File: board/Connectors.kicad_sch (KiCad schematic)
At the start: 17 parts, among them J10 SLOT 1, J11 SLOT 2, J12 SLOT 3, J13 SLOT 4, J14 SLOT 5, J15 AudioJack3, J16 SPI Device 0, J18 SPI Device 1, J19 SPI Device 2, J20 SPI Device 3, J21 SPI Device 4, J22 SPI Device 5, J23 SPI Device 6, J24 SPI Device 7, J25 VIA Port A, J26 SP720APP, J9 SLOT 0

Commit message: Board V1.1G
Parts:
- J15: footprint Connector_Audio:Jack_3.5mm_CUI_SJ1-3523N_Horizontal -> Connector_Audio:Jack_3.5mm_CUI_SJ1-3525N_Horizontal
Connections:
- net A0 renamed A_SLOTS0
- net A1 renamed A_SLOTS1
- net A10 renamed A_SLOTS10
- net A11 renamed A_SLOTS11
- net A12 renamed A_SLOTS12
- net A13 renamed A_SLOTS13
- net A14 renamed A_SLOTS14
- net A15 renamed A_SLOTS15
- net A2 renamed A_SLOTS2
- net A3 renamed A_SLOTS3
- net A4 renamed A_SLOTS4
- net A5 renamed A_SLOTS5
- net A6 renamed A_SLOTS6
- net A7 renamed A_SLOTS7
- net A8 renamed A_SLOTS8
- net A9 renamed A_SLOTS9
- net D0 renamed D_SLOTS0
- net D1 renamed D_SLOTS1
- net D2 renamed D_SLOTS2
- net D3 renamed D_SLOTS3
- net D4 renamed D_SLOTS4
- net D5 renamed D_SLOTS5
- net D6 renamed D_SLOTS6
- net D7 renamed D_SLOTS7
- net RWB renamed P_RWB
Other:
- moved on the sheet: J10, J11, J12, J13, J14, J15, J16, J18, J19, J20, J21, J22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

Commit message: V1.2B: Final for production.
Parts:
- J15: value AudioJack3 -> Audio Jack
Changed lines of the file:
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@@
 		(title "Card-edge and SPI Device Connectors")
 		(date "2025-03-04")
-		(rev "1.1A")
+		(rev "1.3B")
 		(company "Data Tuning")
 		(comment 1 "Hydra 16")
@@
 			)
 		)
-		(property "Value" "AudioJack3"
+		(property "Value" "Audio Jack"
 			(at 200.66 165.7349 0)
 			(effects

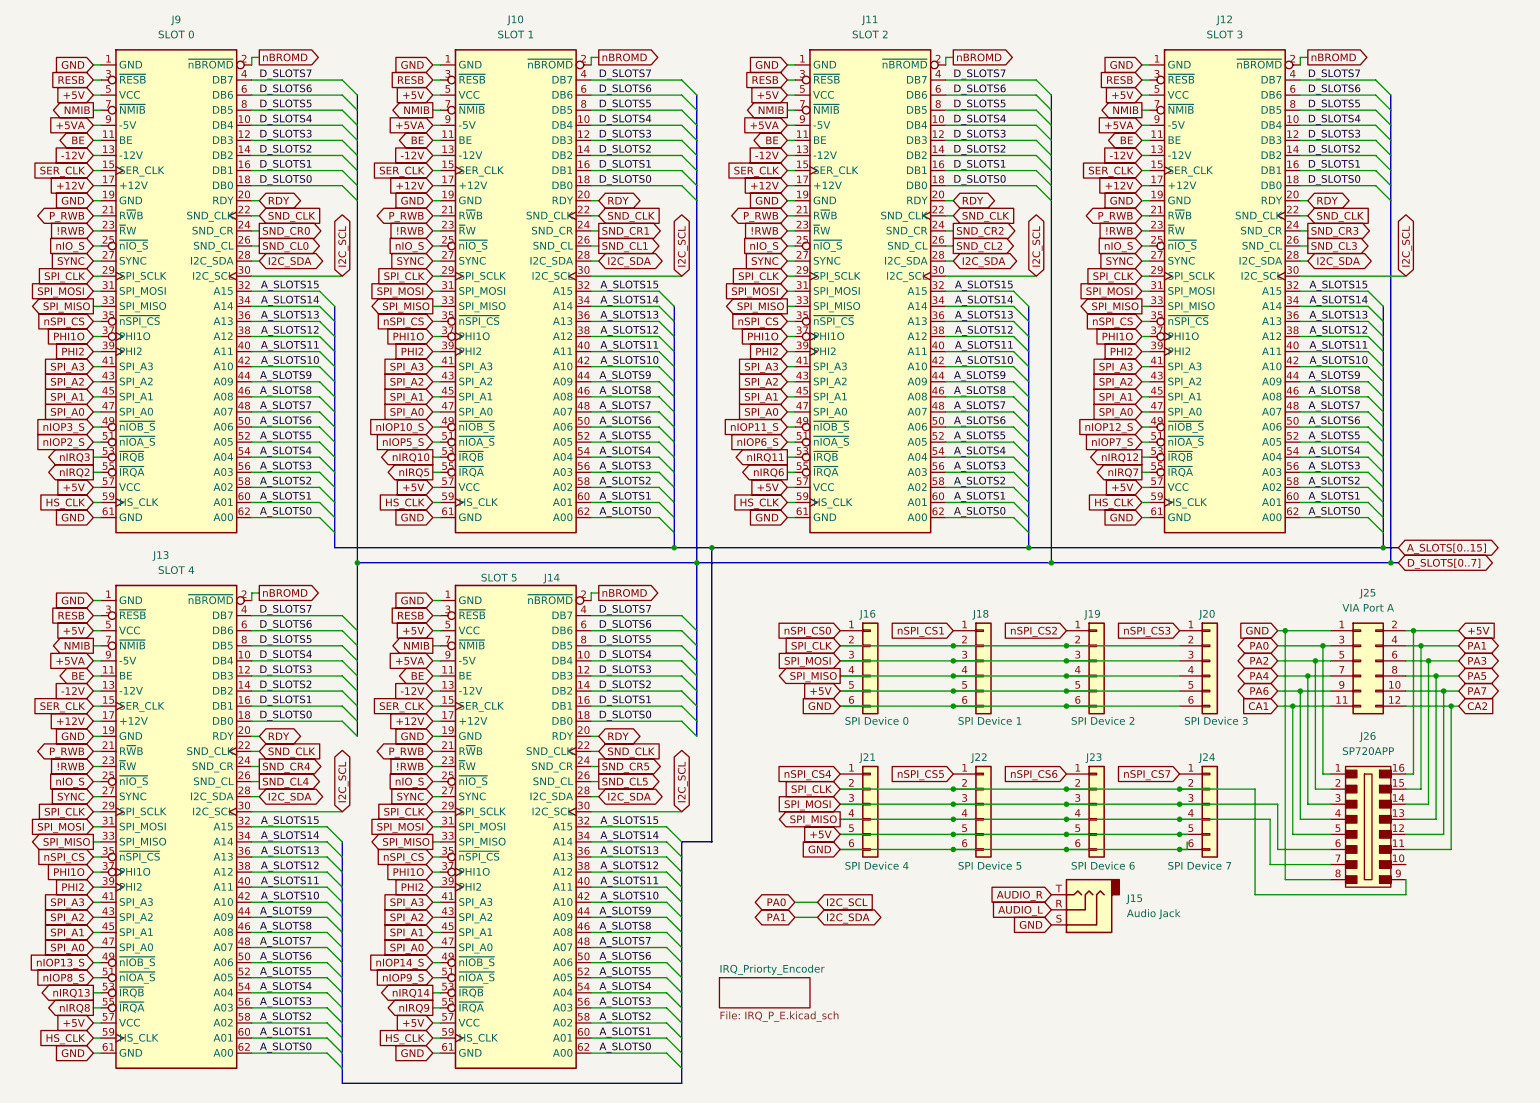
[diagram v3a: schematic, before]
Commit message: V1.3C without board traces
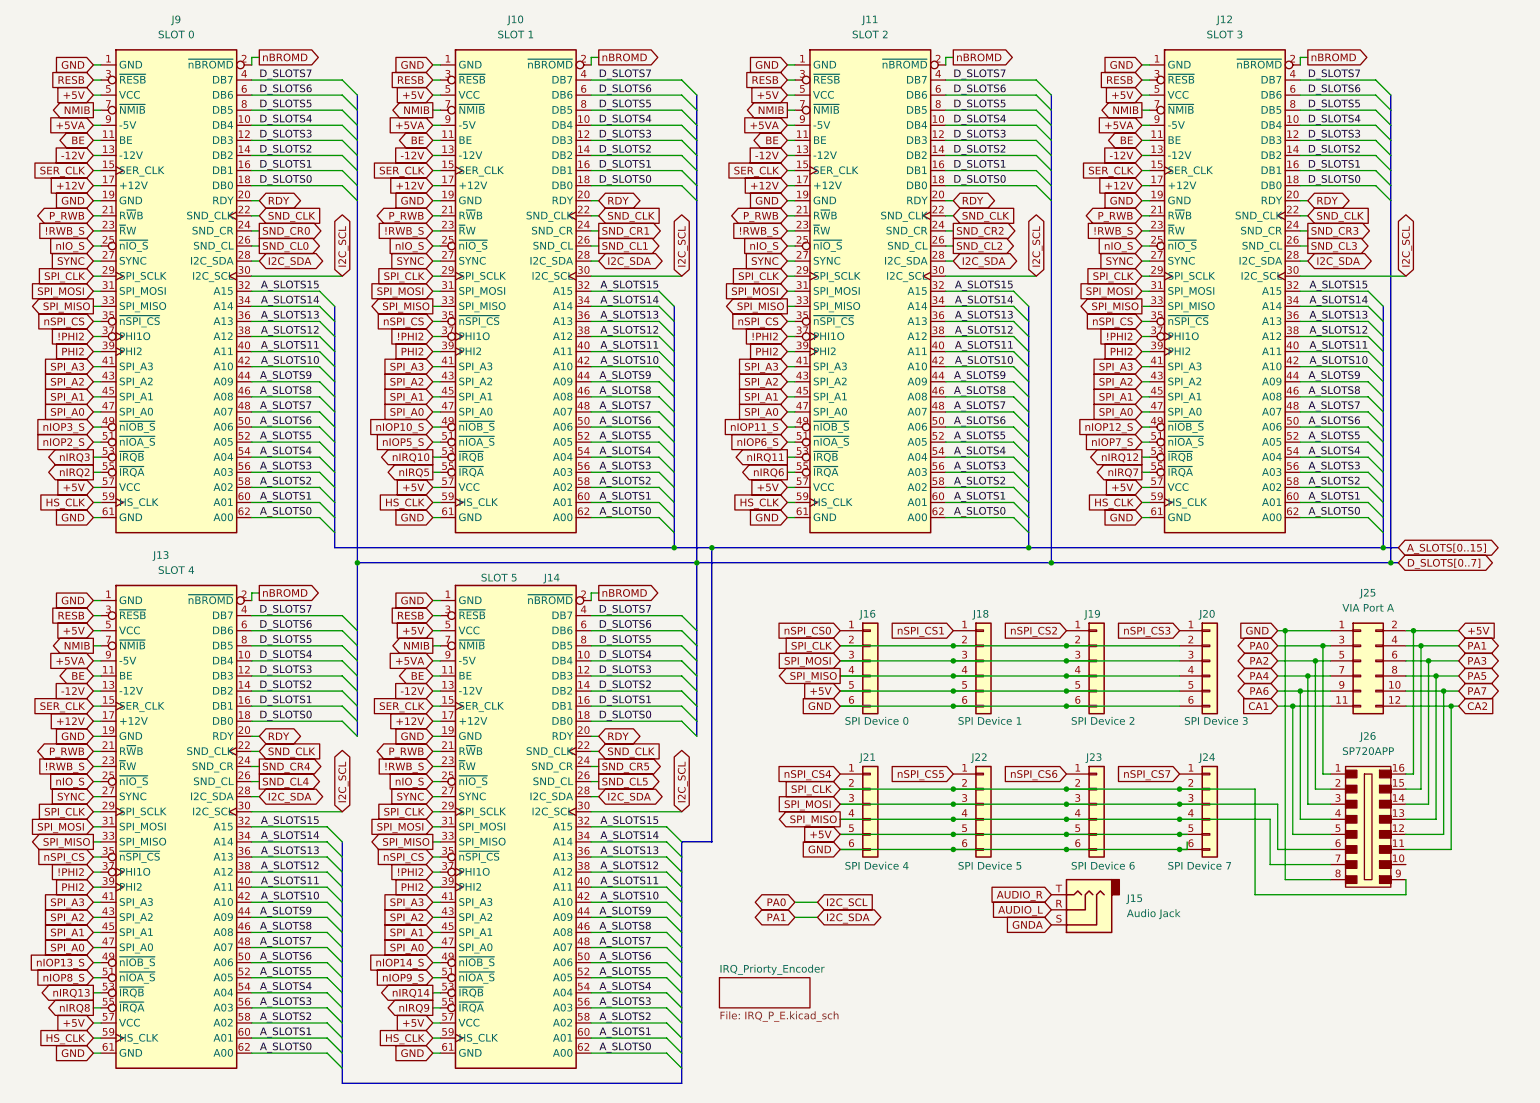
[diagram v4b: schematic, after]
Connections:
- net GND: no longer J15.S
- net !RWB renamed !RWB_S
- net PHI1O renamed !PHI2
- new net GNDA: J15.S
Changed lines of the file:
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@@
 	(title_block
 		(title "Card-edge and SPI Device Connectors")
-		(date "2025-04-15")
-		(rev "1.3")
+		(date "2025-04-23")
+		(rev "1.3C")
 		(company "Data Tuning")
 		(comment 1 "Hydra 16")
@@
 		)
 	)
-	(global_label "PHI1O"
+	(global_label "!PHI2"
 		(shape input)
 		(at 143.51 68.58 180)
@@
 		)
 		(property "Intersheetrefs" "${INTERSHEET_REFS}"
-			(at 134.7795 68.58 0)
+			(at 135.5052 68.58 0)
 			(effects
 				(font
@@
 		)
 	)
-	(global_label "!RWB"
+	(global_label "!RWB_S"
 		(shape input)
 		(at 83.82 140.97 180)
@@
 		)
 		(property "Intersheetrefs" "${INTERSHEET_REFS}"
-			(at 76.2386 140.97 0)
+			(at 74.0615 140.97 0)
 			(effects
 				(font
@@
 		)
 	)
-	(global_label "!RWB"
+	(global_label "!RWB_S"
 		(shape input)
 		(at 26.67 140.97 180)
@@
 		)
 		(property "Intersheetrefs" "${INTERSHEET_REFS}"
-			(at 19.0886 140.97 0)
+			(at 16.9115 140.97 0)
 			(effects
 				(font
@@
 		)
 	)
-	(global_label "PHI1O"
+	(global_label "!PHI2"
 		(shape input)
 		(at 83.82 68.58 180)
@@
 		)
 		(property "Intersheetrefs" "${INTERSHEET_REFS}"
-			(at 75.0895 68.58 0)
+			(at 75.8152 68.58 0)
 			(effects
 				(font
@@
 		)
 	)
-	(global_label "GND"
+	(global_label "GNDA"
 		(shape input)
 		(at 187.96 167.64 180)
@@
 		)
 		(property "Intersheetrefs" "${INTERSHEET_REFS}"
-			(at 181.1043 167.64 0)
+			(at 180.0157 167.64 0)
 			(effects
 				(font
@@
 		)
 	)
-	(global_label "!RWB"
+	(global_label "!RWB_S"
 		(shape input)
 		(at 203.2 50.8 180)
@@
 		)
 		(property "Intersheetrefs" "${INTERSHEET_REFS}"
-			(at 195.6186 50.8 0)
+			(at 193.4415 50.8 0)
 			(effects
 				(font
@@
 		)
 	)
-	(global_label "PHI1O"
+	(global_label "!PHI2"
 		(shape input)
 		(at 26.67 68.58 180)
@@
 		)
 		(property "Intersheetrefs" "${INTERSHEET_REFS}"
-			(at 17.9395 68.58 0)
+			(at 18.6652 68.58 0)
 			(effects
 				(font
@@
 		)
 	)
-	(global_label "!RWB"
+	(global_label "!RWB_S"
 		(shape input)
 		(at 26.67 50.8 180)
@@
 		)
 		(property "Intersheetrefs" "${INTERSHEET_REFS}"
-			(at 19.0886 50.8 0)
+			(at 16.9115 50.8 0)
 			(effects
 				(font
@@
 		)
 	)
-	(global_label "PHI1O"
+	(global_label "!PHI2"
 		(shape input)
 		(at 203.2 68.58 180)
@@
 		)
 		(property "Intersheetrefs" "${INTERSHEET_REFS}"
-			(at 194.4695 68.58 0)
+			(at 195.1952 68.58 0)
 			(effects
 				(font
@@
 		)
 	)
-	(global_label "PHI1O"
+	(global_label "!PHI2"
 		(shape input)
 		(at 26.67 158.75 180)
@@
 		)
 		(property "Intersheetrefs" "${INTERSHEET_REFS}"
-			(at 17.9395 158.75 0)
+			(at 18.6652 158.75 0)
 			(effects
 				(font
@@
 		)
 	)
-	(global_label "!RWB"
+	(global_label "!RWB_S"
 		(shape input)
 		(at 83.82 50.8 180)
@@
 		)
 		(property "Intersheetrefs" "${INTERSHEET_REFS}"
-			(at 76.2386 50.8 0)
+			(at 74.0615 50.8 0)
 			(effects
 				(font
@@
 		)
 	)
-	(global_label "PHI1O"
+	(global_label "!PHI2"
 		(shape input)
 		(at 83.82 158.75 180)
@@
 		)
 		(property "Intersheetrefs" "${INTERSHEET_REFS}"
-			(at 75.0895 158.75 0)
+			(at 75.8152 158.75 0)
 			(effects
 				(font
@@
 		)
 	)
-	(global_label "!RWB"
+	(global_label "!RWB_S"
 		(shape input)
 		(at 143.51 50.8 180)
@@
 		)
 		(property "Intersheetrefs" "${INTERSHEET_REFS}"
-			(at 135.9286 50.8 0)
+			(at 133.7515 50.8 0)
 			(effects
 				(font

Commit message: V1.4E
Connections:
- net A_SLOTS0 renamed A0
- net A_SLOTS1 renamed A1
- net A_SLOTS10 renamed A10
- net A_SLOTS11 renamed A11
- net A_SLOTS12 renamed A12
- net A_SLOTS13 renamed A13
- net A_SLOTS14 renamed A14
- net A_SLOTS15 renamed A15
- net A_SLOTS2 renamed A2
- net A_SLOTS3 renamed A3
- net A_SLOTS4 renamed A4
- net A_SLOTS5 renamed A5
- net A_SLOTS6 renamed A6
- net A_SLOTS7 renamed A7
- net A_SLOTS8 renamed A8
- net A_SLOTS9 renamed A9
- net D_SLOTS0 renamed D0
- net D_SLOTS1 renamed D1
- net D_SLOTS2 renamed D2
- net D_SLOTS3 renamed D3
- net D_SLOTS4 renamed D4
- net D_SLOTS5 renamed D5
- net D_SLOTS6 renamed D6
- net D_SLOTS7 renamed D7

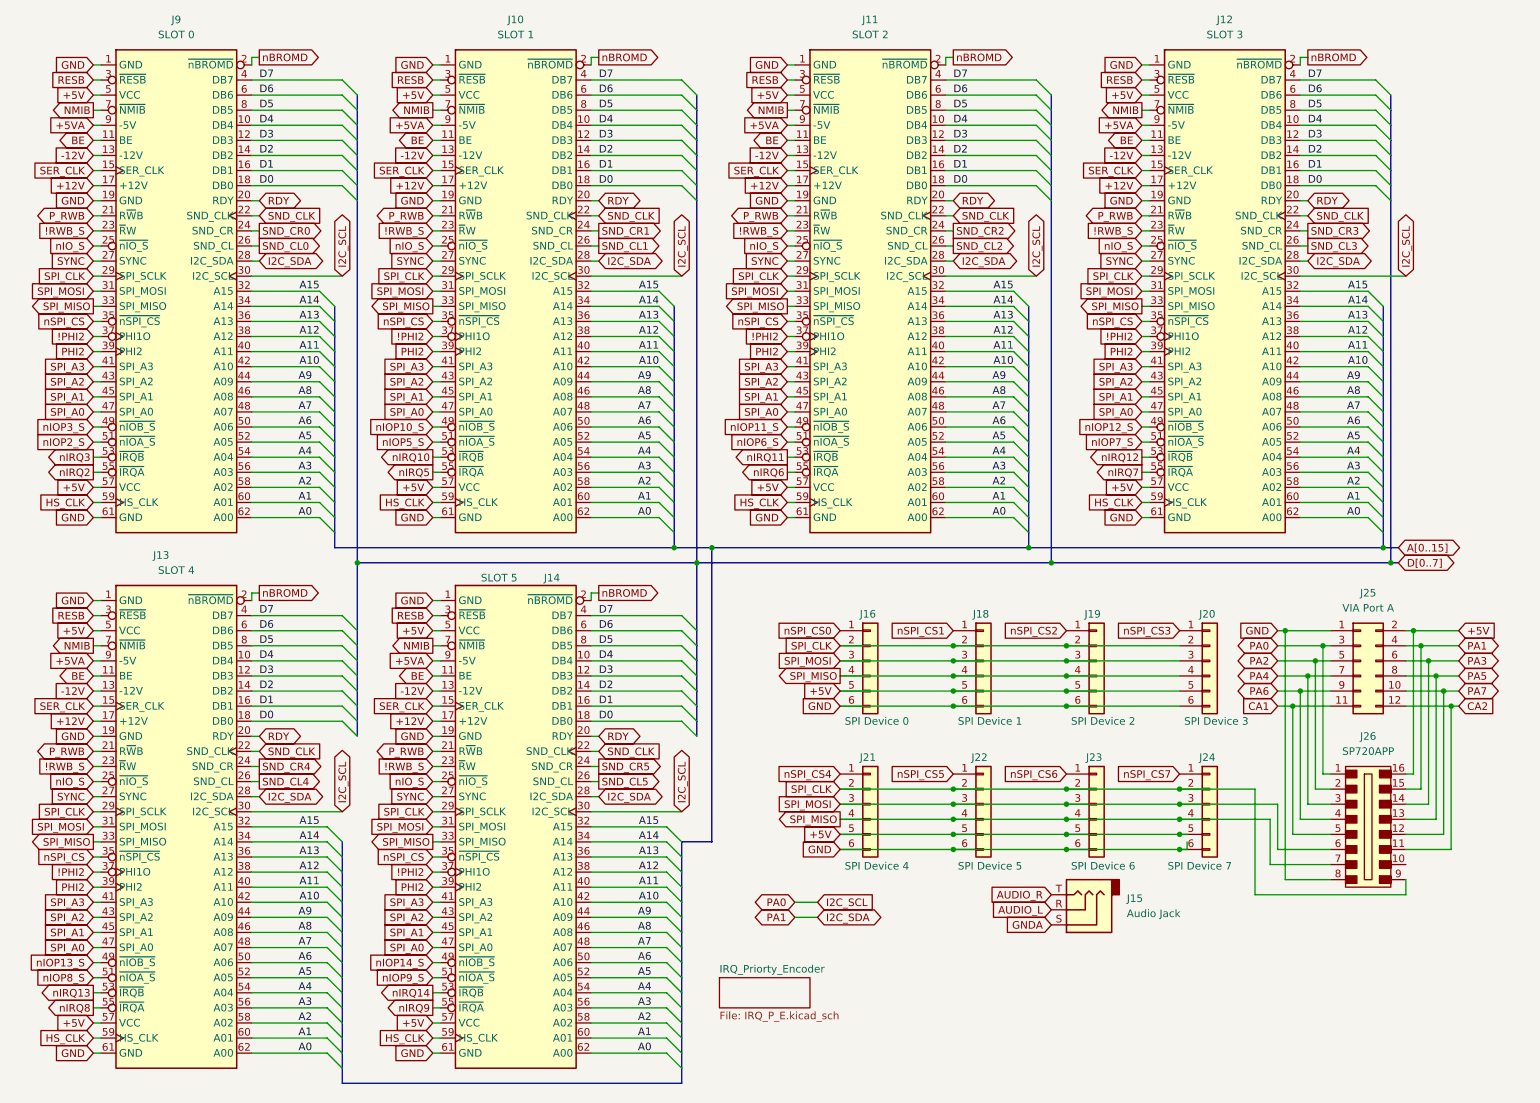
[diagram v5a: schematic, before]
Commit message: Version 1.7A: More rearrangement, partial wiring of PDB, addition of W register
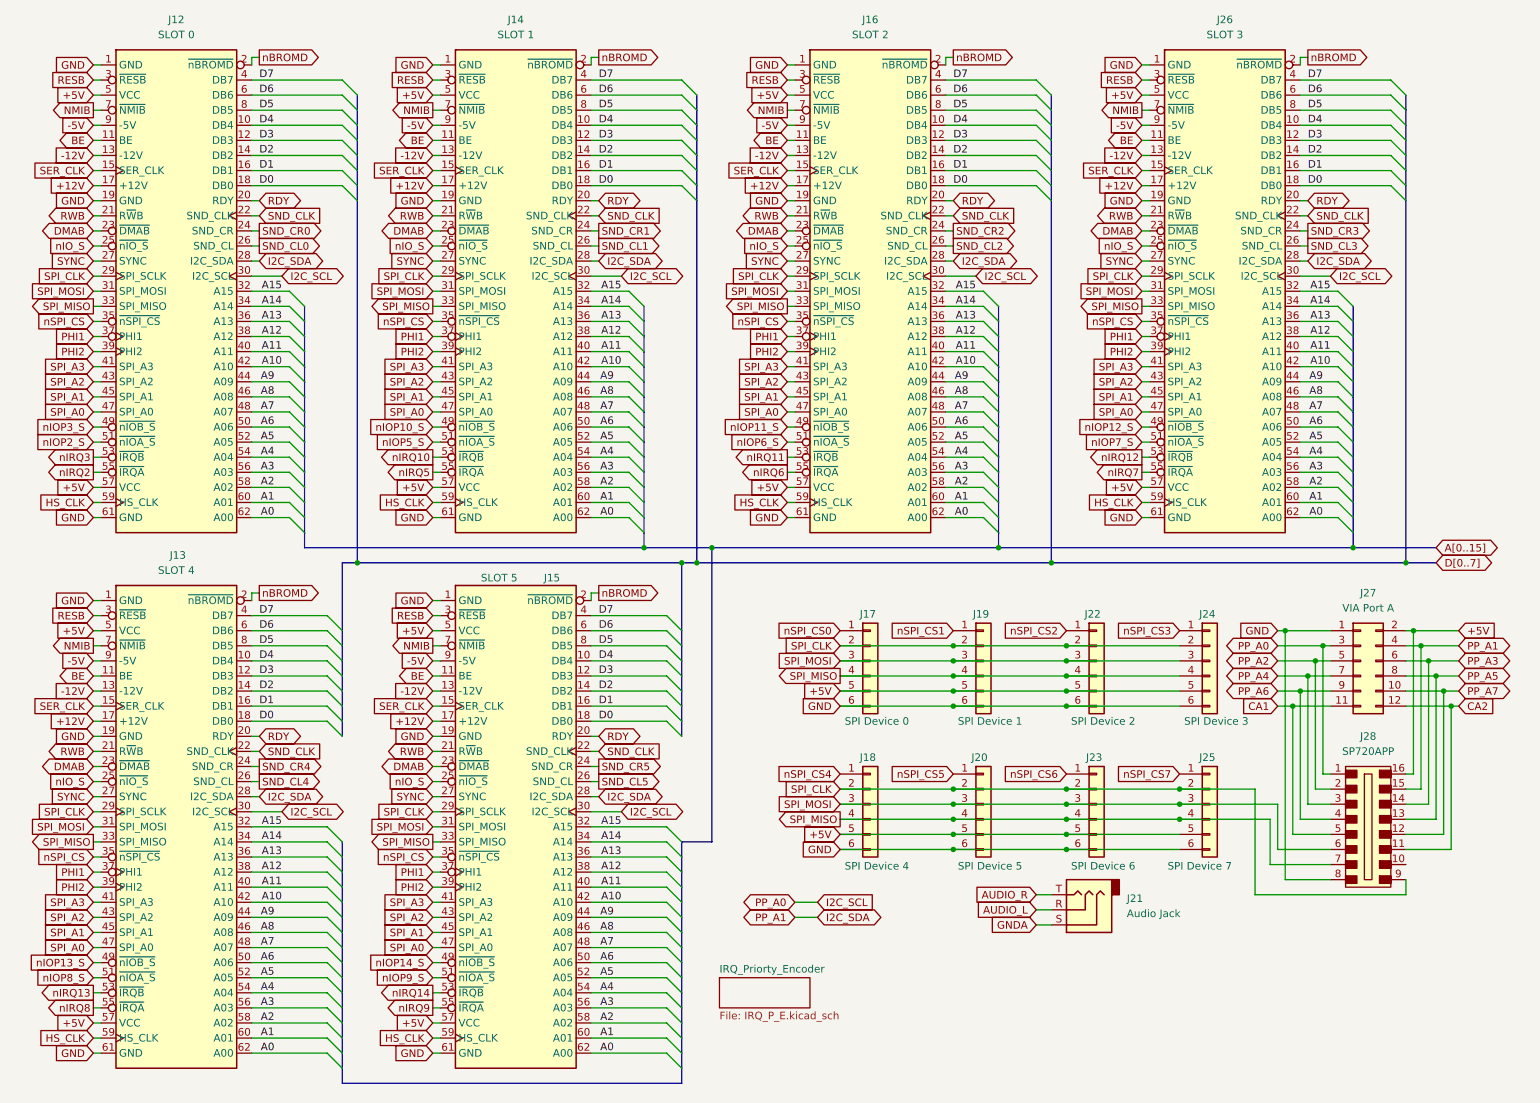
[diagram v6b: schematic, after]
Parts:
- renumbered J9 to J12, J10 to J14, J14 to J15, J11 to J16, J16 to J17, J21 to J18, J18 to J19, J22 to J20, J15 to J21, J19 to J22, J20 to J24, J24 to J25, J12 to J26, J25 to J27, J26 to J28
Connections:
- net !PHI2 renamed PHI1
- net !RWB_S renamed DMAB
- net +5VA renamed -5V
- net PA2 renamed PP_A2
- net PA3 renamed PP_A3
- net PA4 renamed PP_A4
- net PA5 renamed PP_A5
- net PA6 renamed PP_A6
- net PA7 renamed PP_A7
- net P_RWB renamed RWB

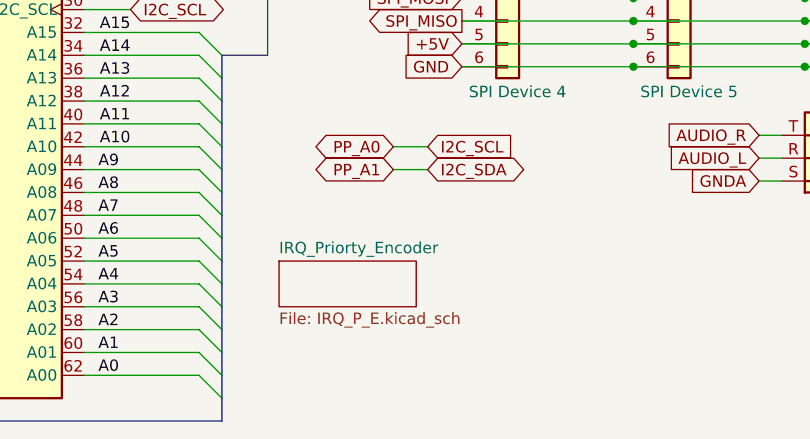
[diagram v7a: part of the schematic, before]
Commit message: 1.7C: Logic corrections and placement tweaks
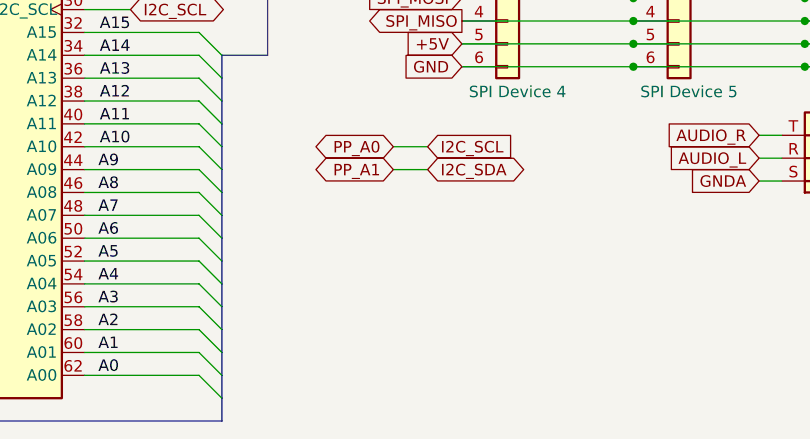
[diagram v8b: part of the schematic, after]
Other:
- removed sheet IRQ_Priorty_Encoder
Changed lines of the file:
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@@
 	(title_block
 		(title "Card-edge and SPI Device Connectors")
-		(date "2025-09-18")
-		(rev "1.7A")
+		(date "2025-10-01")
+		(rev "1.7C")
 		(company "Data Tuning")
 		(comment 1 "Hydra 16")
@@
 				)
 			)
-		)
-	)
-	(sheet
-		(at 132.08 176.53)
-		(size 15.24 5.08)
-		(exclude_from_sim no)
-		(in_bom yes)
-		(on_board yes)
-		(dnp no)
-		(fields_autoplaced yes)
-		(stroke
-			(width 0.1524)
-			(type solid)
-		)
-		(fill
-			(color 0 0 0 0.0000)
-		)
-		(property "Sheetname" "IRQ_Priorty_Encoder"
-			(at 132.08 175.8184 0)
-			(effects
-				(font
-					(size 1.27 1.27)
-				)
-				(justify left bottom)
-			)
-		)
-		(property "Sheetfile" "IRQ_P_E.kicad_sch"
-			(at 132.08 182.1946 0)
-			(effects
-				(font
-					(size 1.27 1.27)
-				)
-				(justify left top)
-			)
-		)
-		(instances
-			(project "hydra-16"
-				(path "/ef29fc71-3fec-48b5-8a1a-46bee537a98c/9e82ed5b-af5c-4fee-b6ce-87e97255963b"
-					(page "8")
-				)
-			)
